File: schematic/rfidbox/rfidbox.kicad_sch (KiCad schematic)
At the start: 7 parts, among them J1 Raspberry_Pi_4, J2 Conn_01x02_Pin, U1 ADS1115IDGS

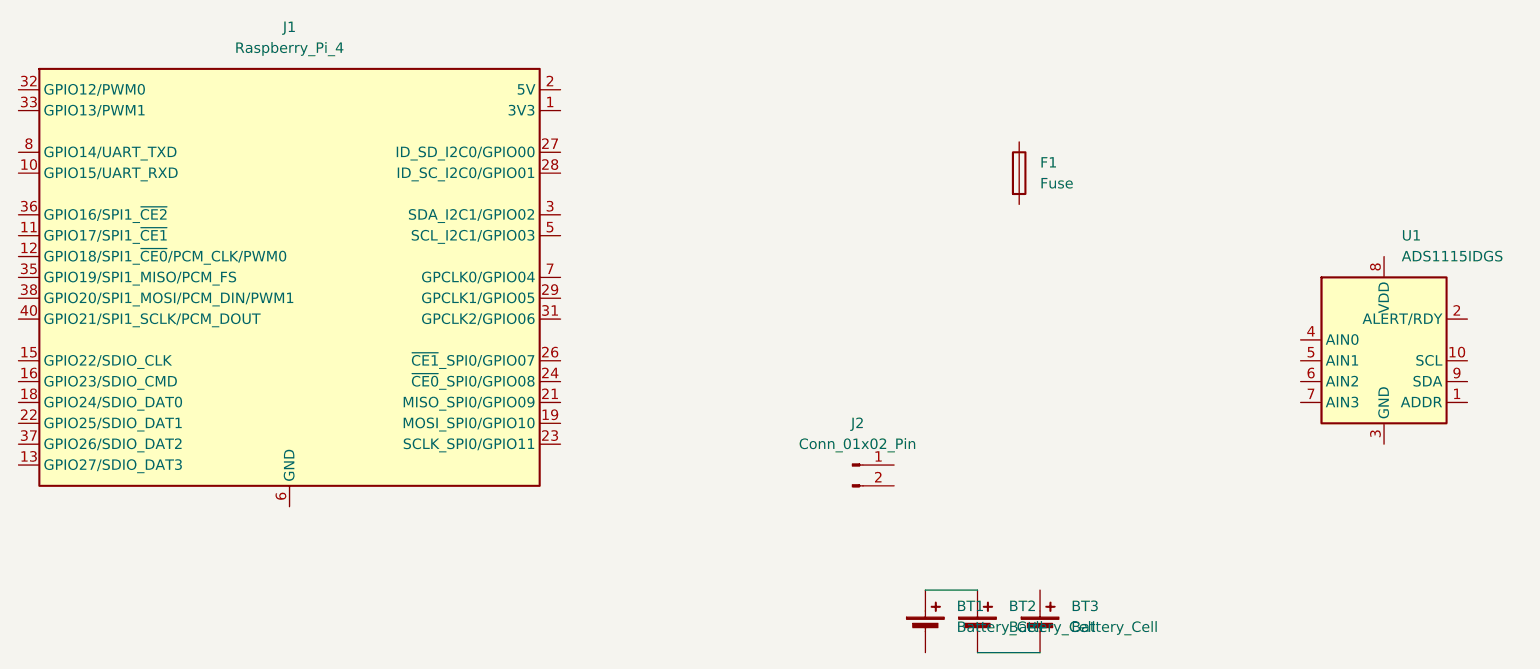
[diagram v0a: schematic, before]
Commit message: fixed timers, added gpio button,
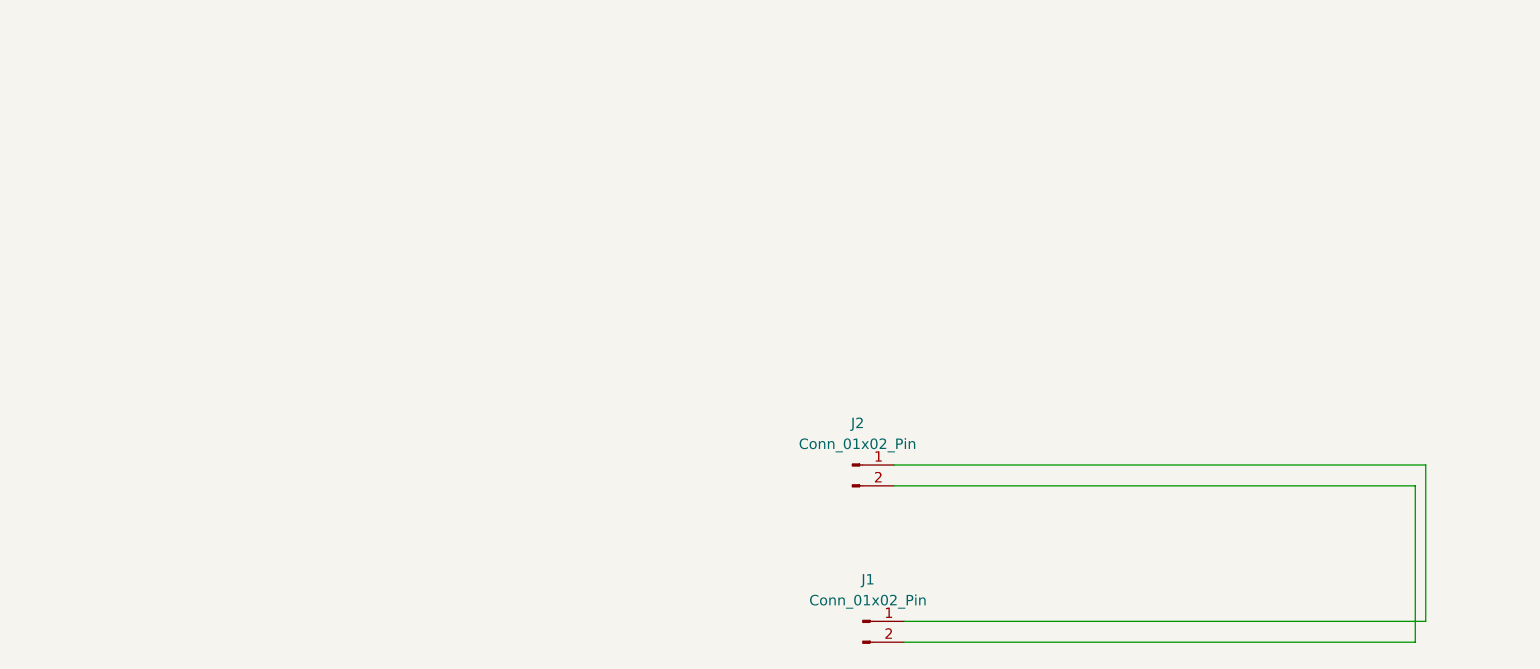
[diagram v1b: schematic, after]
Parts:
- removed BT1, BT2, BT3: Battery_Cell, symbol Device:Battery_Cell
- removed F1: Fuse, symbol Device:Fuse
- removed J1: Raspberry_Pi_4, symbol Connector:Raspberry_Pi_4
- removed U1: ADS1115IDGS, Package_SO:TSSOP-10_3x3mm_P0.5mm, symbol Analog_ADC:ADS1115IDGS
- added J1: Conn_01x02_Pin, Connector_JST:JST_VH_B2P-VH-B_1x02_P3.96mm_Vertical, symbol Connector:Conn_01x02_Pin
- J2: footprint (none) -> Connector_JST:JST_VH_B2P-VH-B_1x02_P3.96mm_Vertical
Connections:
- net at J2.1 (Pin_1): now also J1.1 (Pin_1)
- net at J2.2 (Pin_2): now also J1.2 (Pin_2)
